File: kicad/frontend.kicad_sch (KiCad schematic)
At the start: 10 parts, among them U201 TLV3603DCK

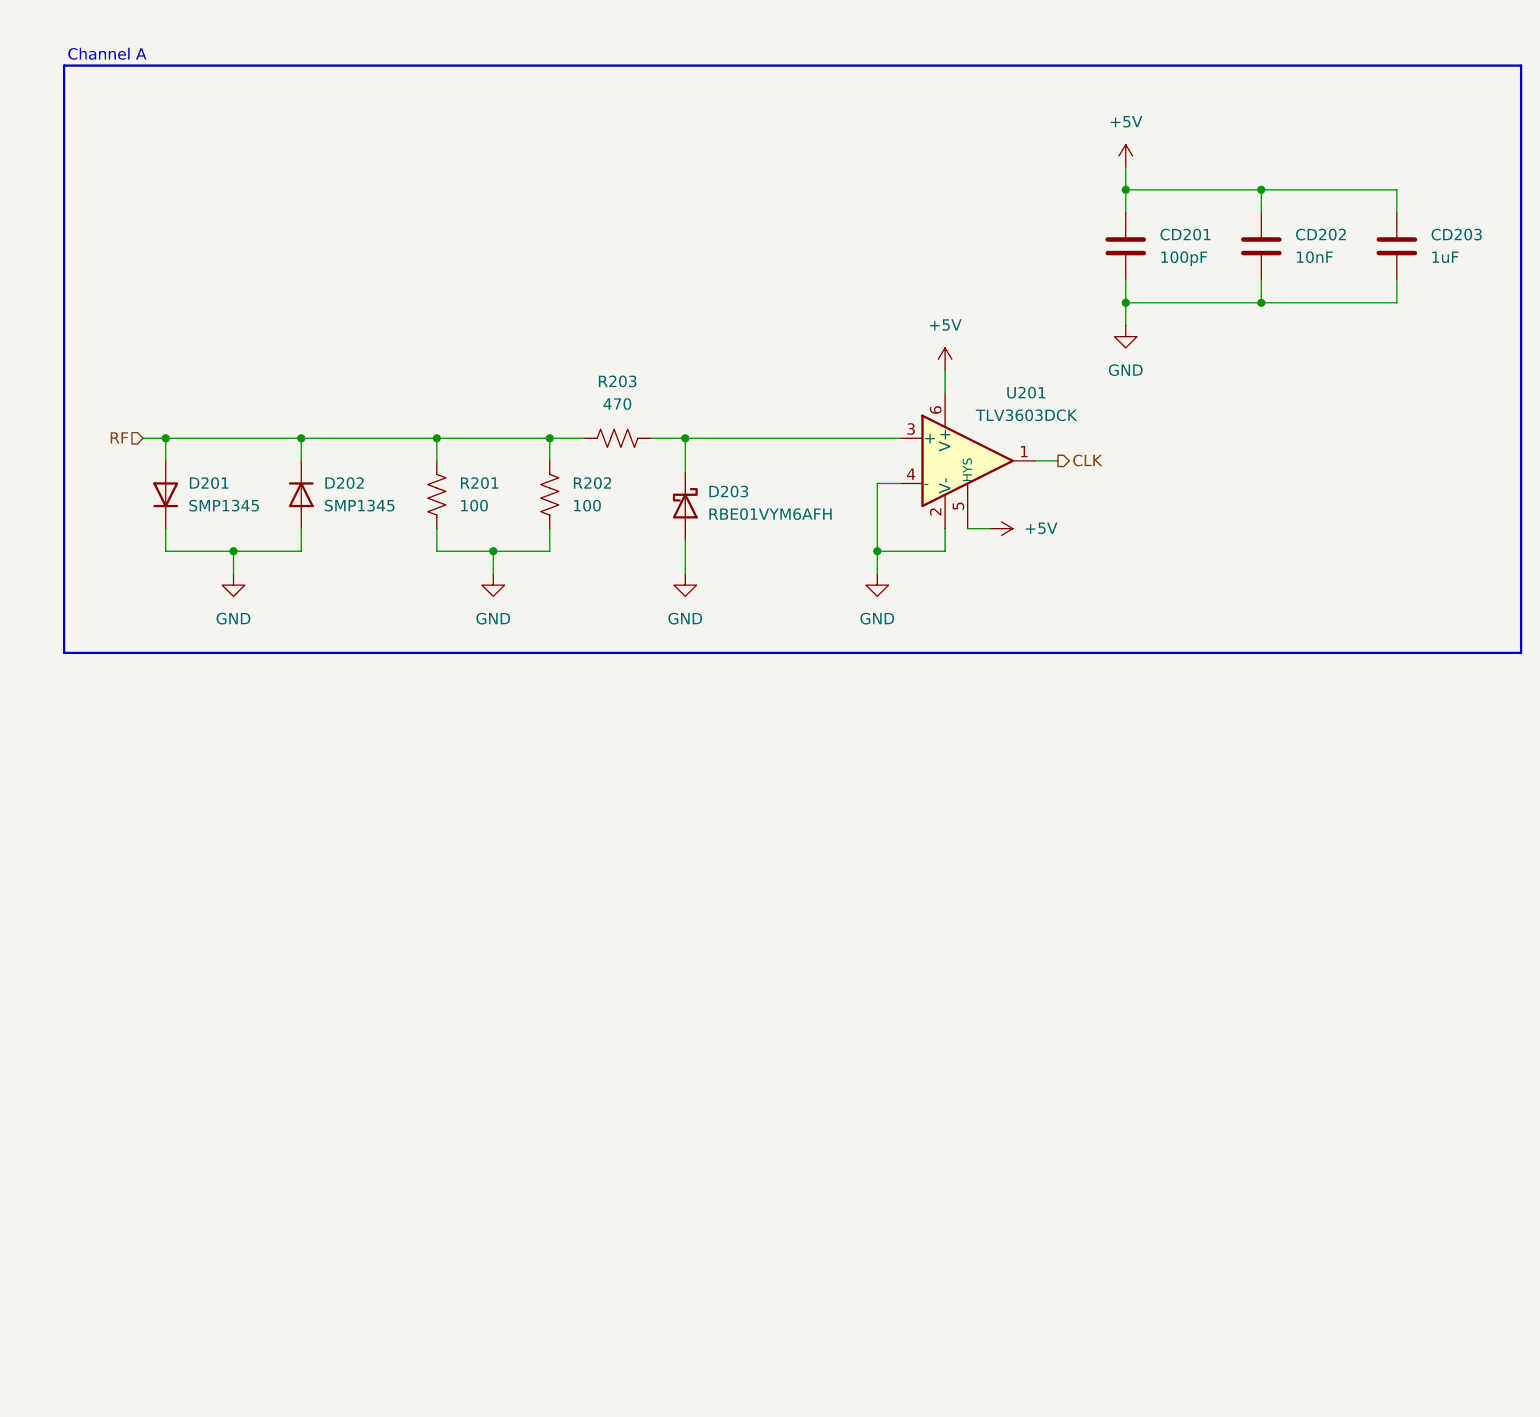
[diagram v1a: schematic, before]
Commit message: split frontend into two channels
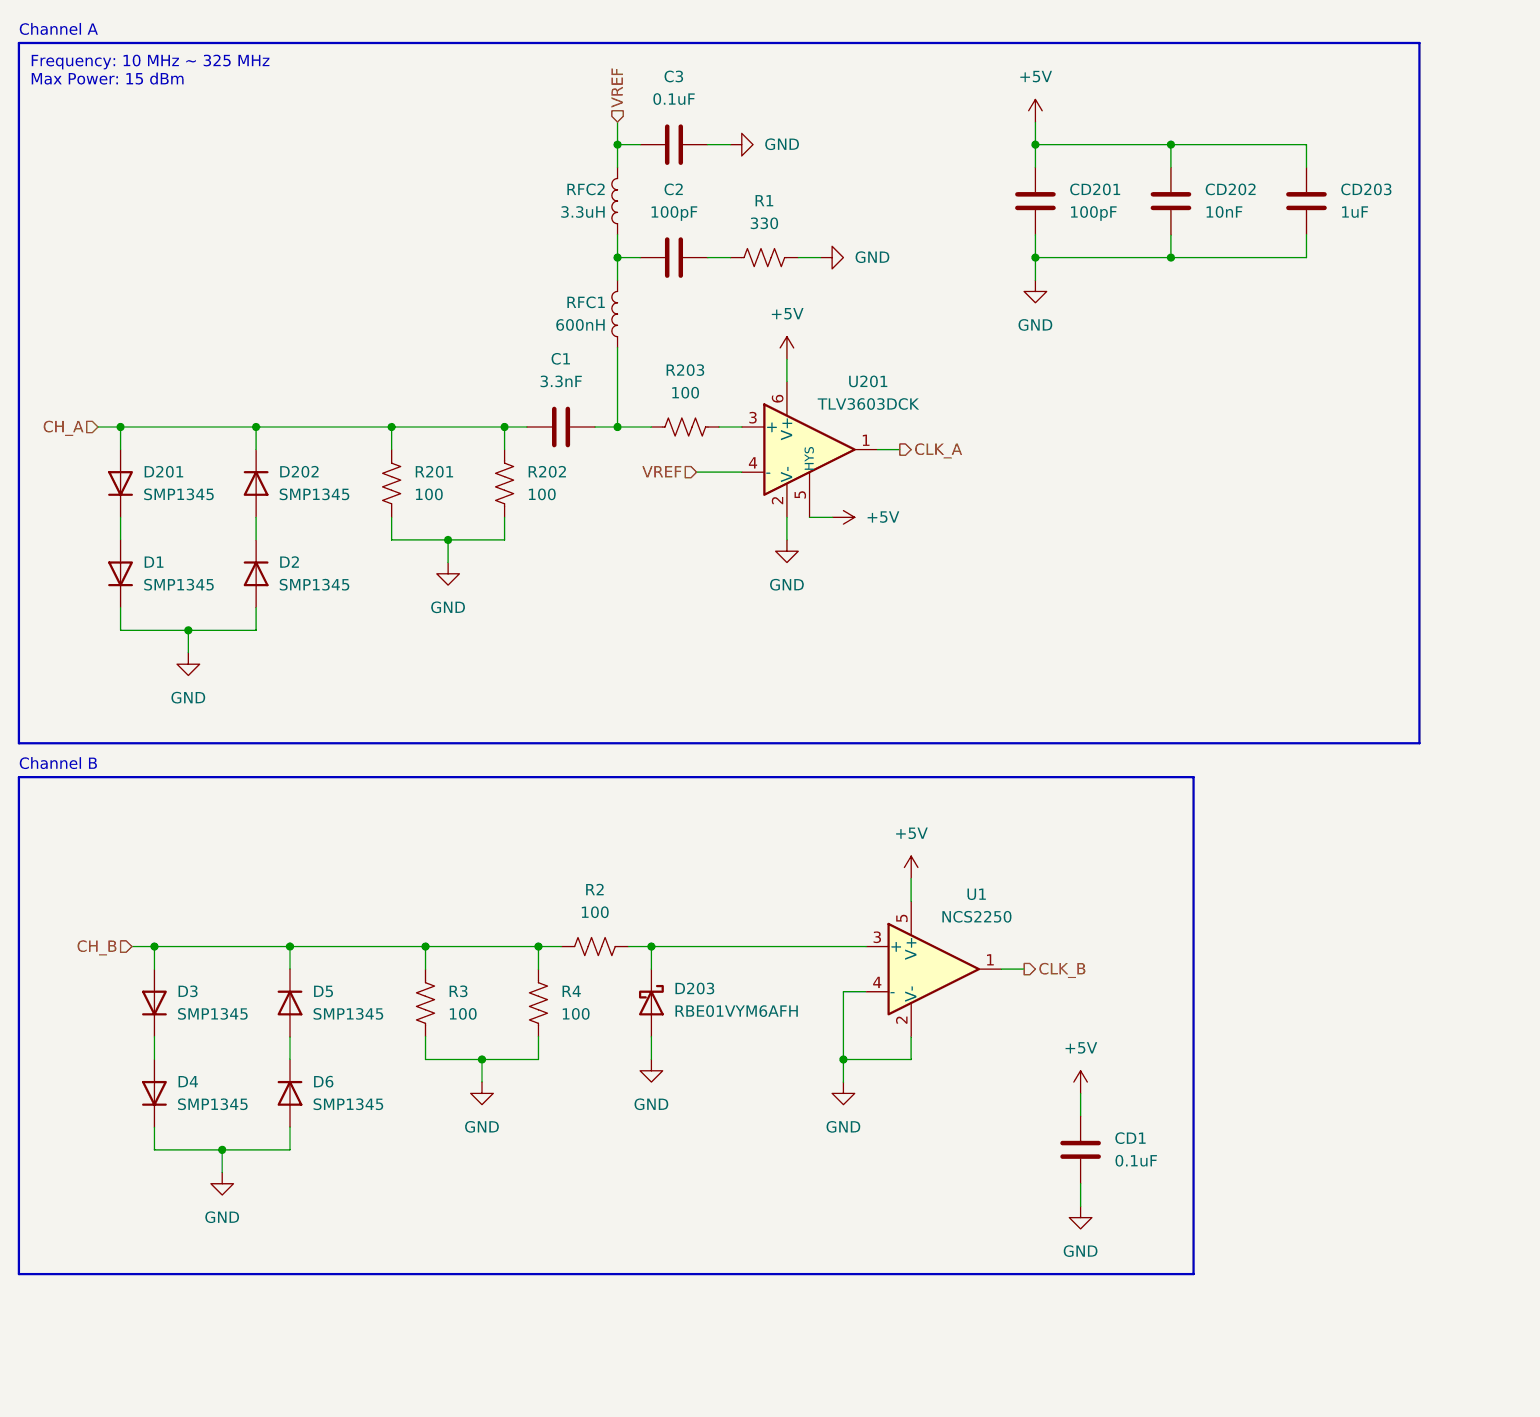
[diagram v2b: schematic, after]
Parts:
- added C1: 3.3nF, symbol Device:C
- added C2: 100pF, symbol Device:C
- added C3: 0.1uF, symbol Device:C
- added CD1: 0.1uF, Custom:C_0402_1005Metric_Fix, symbol Device:C
- added D1, D2, D3, D4, D5, D6: SMP1345, Diode_SMD:D_0402_1005Metric_Pad0.77x0.64mm_HandSolder, symbol Device:D
- added R1: 330, symbol Device:R_US
- added R2: 100, Custom:R_0402_1005Metric_Fix, symbol Device:R_US
- added R3, R4: 100, Resistor_SMD:R_1206_3216Metric, symbol Device:R_US
- added RFC1: 600nH, symbol Device:L
- added RFC2: 3.3uH, symbol Device:L
- added U1: NCS2250, Package_SO:TSOP-5_1.65x3.05mm_P0.95mm, symbol Custom:NCS2250
- R203: value 470 -> 100
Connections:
- net +5V: now also CD1.1, U1.5 (V+)
- net GND: now also C3.2, CD1.2, D1.1 (K), D2.2 (A), D4.1 (K), D6.2 (A), R1.2, R3.1, R4.1, U1.2 (V-), U1.4 (-); no longer D201.1 (K), D202.2 (A), U201.4 (-)
- net at R203.2, U201.3 (+): no longer D203.1 (K)
- net CLK renamed CLK_A
- net RF renamed CH_A
- net CH_A: now also C1.1; no longer R203.1
- new net: D1.2 (A), D201.1 (K)
- new net: D203.1 (K), R2.2, U1.3 (+)
- new net: D2.1 (K), D202.2 (A)
- new net: C1.2, R203.1, RFC1.2
- new net: C2.1, RFC1.1, RFC2.2
- new net: C2.2, R1.1
- new net: D5.2 (A), D6.1 (K)
- new net: D3.1 (K), D4.2 (A)
- new net CH_B: D3.2 (A), D5.1 (K), R2.1, R3.2, R4.2
- new net CLK_B: U1.1
- new net VREF: C3.1, RFC2.1, U201.4 (-)
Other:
- note added: "Channel B"
- note added: "Frequency: 10 MHz ~ 325 MHz Max Power: 15 dBm"
- moved on the sheet: CD201, CD202, CD203, D201, D202, D203, R201, R202, R203, U201

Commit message: ch a voltage reference, ch b hysteresis
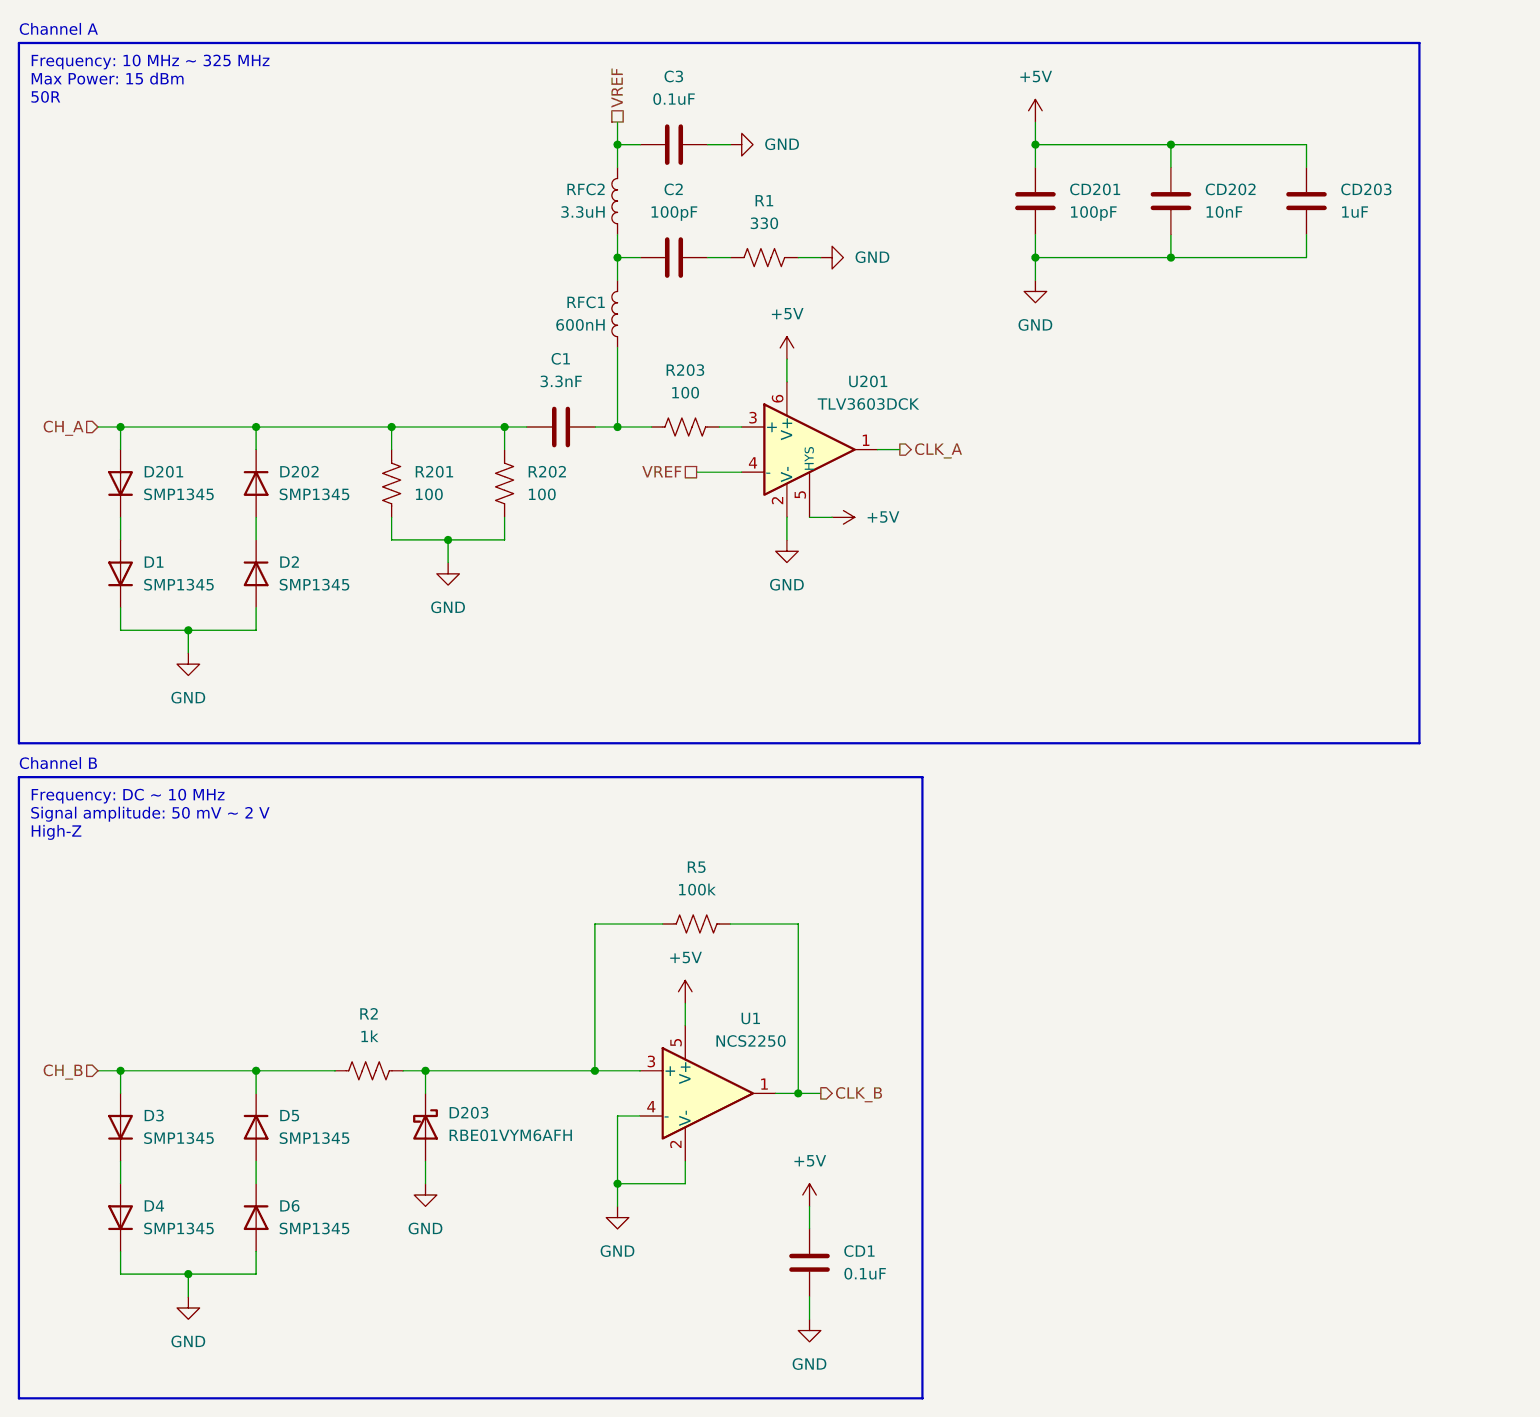
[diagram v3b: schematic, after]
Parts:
- removed R3, R4: 100, Resistor_SMD:R_1206_3216Metric, symbol Device:R_US
- added R5: 100k, Custom:R_0402_1005Metric_Fix, symbol Device:R_US
- R2: value 100 -> 1k
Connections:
- net CLK_B: now also R5.2
- net at D203.1 (K), R2.2, U1.3 (+): now also R5.1
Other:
- note added: "Frequency: 10 MHz ~ 325 MHz Max Power: 15 dBm 50R"
- note added: "Frequency: DC ~ 10 MHz Signal amplitude: 50 mV ~ 2 V High-Z"
- note removed: "Frequency: 10 MHz ~ 325 MHz Max Power: 15 dBm"
- moved on the sheet: CD1, D203, D3, D4, D5, D6, R2, U1

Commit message: rework frontend, channel gating
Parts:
- U201: symbol custom:TLV3603DCK -> Custom:TLV3603DCK
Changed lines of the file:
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@@
 	)
 	(symbol
-		(lib_id "custom:TLV3603DCK")
+		(lib_id "Custom:TLV3603DCK")
 		(at 102.87 62.23 0)
 		(unit 1)
